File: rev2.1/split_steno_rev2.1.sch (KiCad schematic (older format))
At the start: 59 parts, among them J1 USB_OTG, J2 Audio-Jack-4, P1 TC2030-IDC, SW1 SW_Push, SW10 SW_Push, SW11 SW_Push, SW12 SW_Push, SW13 SW_Push, SW14 SW_Push, SW15 SW_Push, SW16 SW_Push, SW17 SW_Push, SW18 SW_Push, SW19 SW_Push, SW2 SW_Push, SW20 SW_Push, SW21 SW_Push, SW22 Switch-6P-2S2T, SW3 SW_Push, SW4 SW_Push, SW5 SW_Push, SW6 SW_Push, SW7 SW_Push, SW8 SW_Push, SW9 SW_Push, U1 74LVC1G34, U4 MCP1700, U5 ATXMEGA128A4U-AU, U6 nRF24L01_module

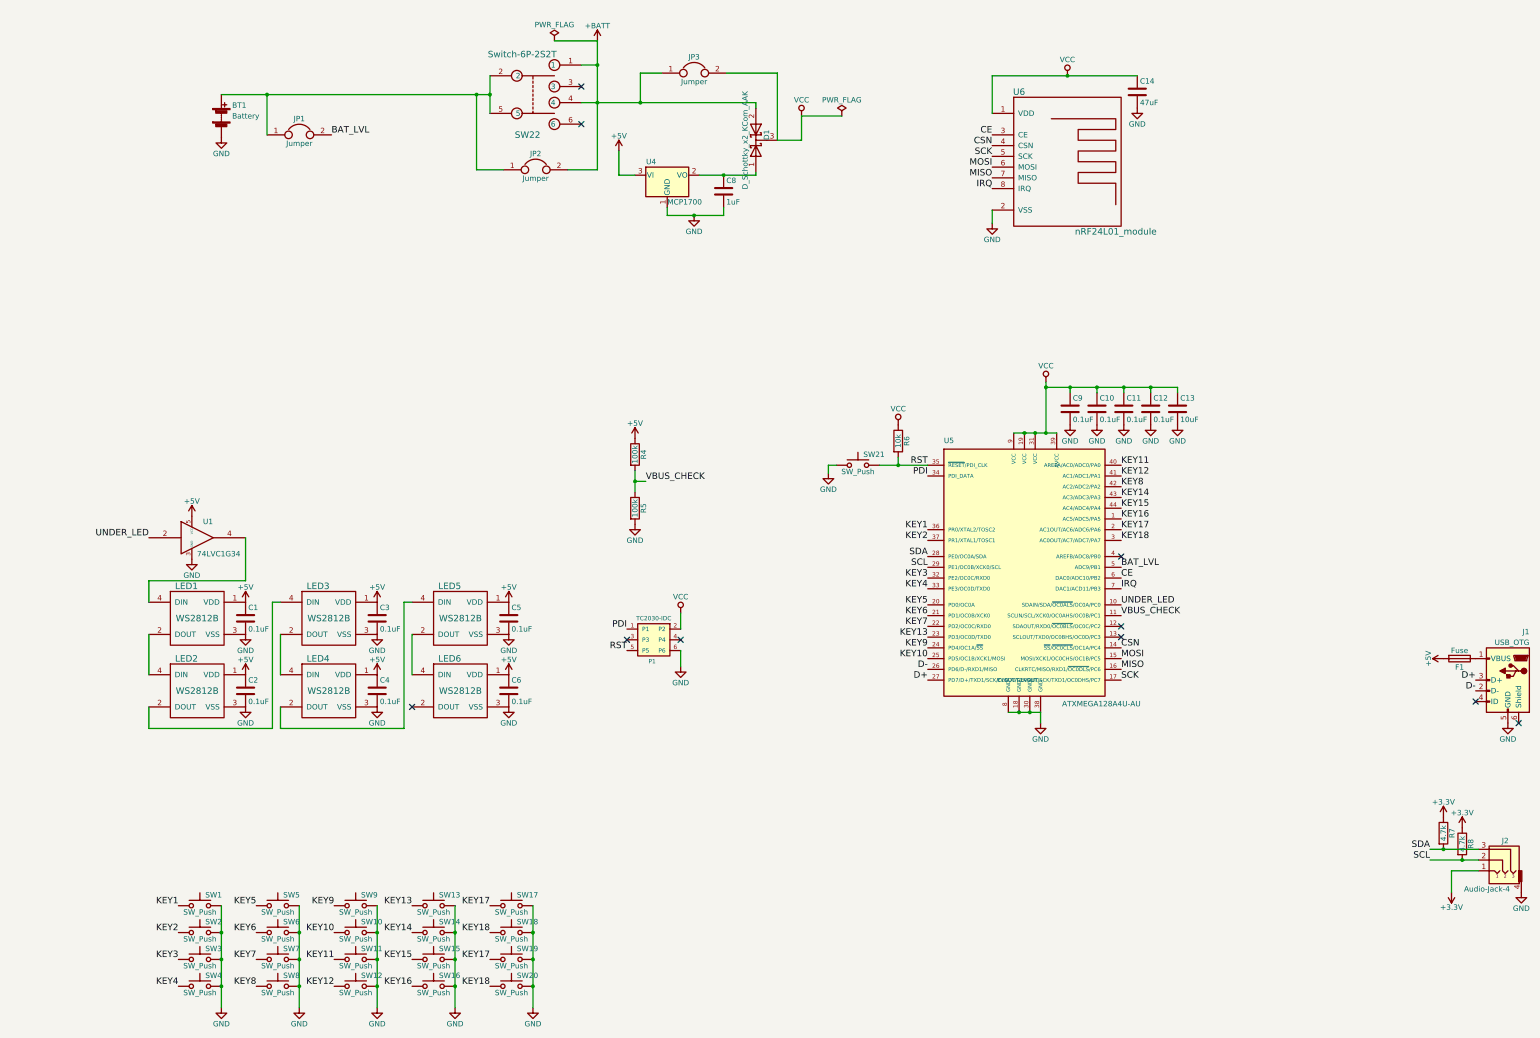
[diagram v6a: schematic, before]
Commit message: reorganized pins, removed NO USB jumper
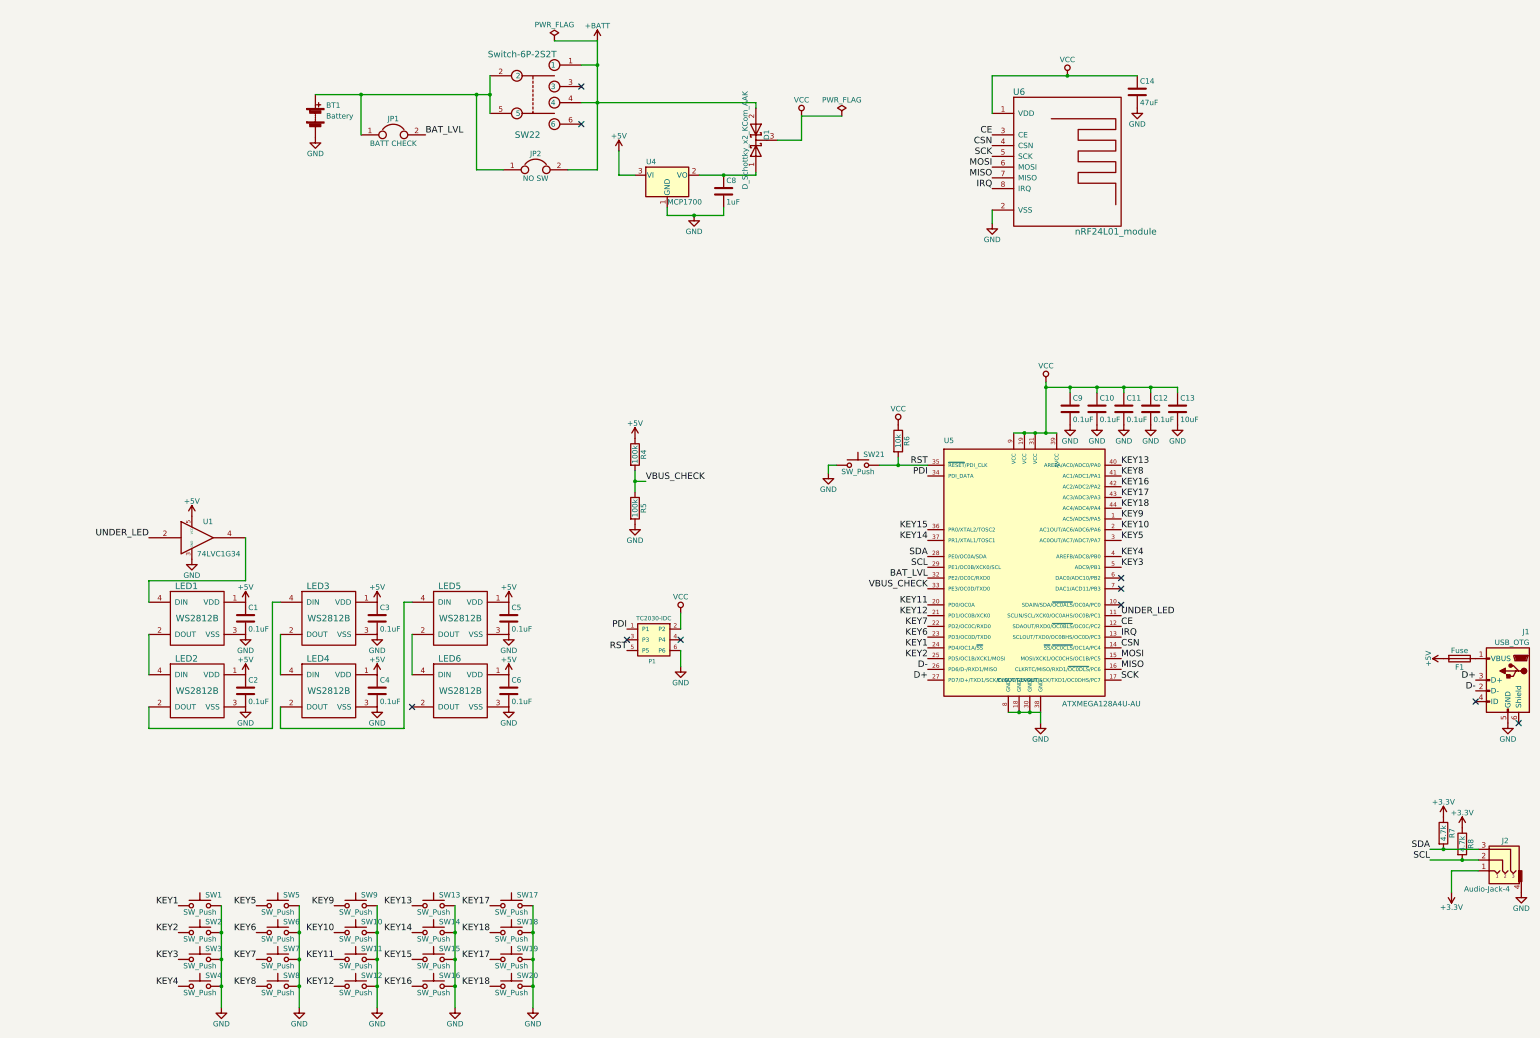
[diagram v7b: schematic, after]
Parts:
- removed JP3: Jumper, jumper:Jumper_1x02_P2.54mm_THT, symbol Jumper
- JP1: value Jumper -> BATT CHECK
- JP2: value Jumper -> NO SW
- P1: footprint Tag-Connect:TC2030-NL_SMALL_AND_IDC_PDI_Extra_Pads -> Tag-Connect:TC2030-NL_SMALL_AND_IDC_PDI
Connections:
- net BAT_LVL: now also U5.32 (PE2/OC0C/RXD0); no longer U5.5 (ADC9/PB1)
- net CE: now also U5.12 (SDAOUT/RXD0/~OC0BLS~/OC0C/PC2); no longer U5.6 (DAC0/ADC10/PB2)
- net IRQ: now also U5.13 (SCLOUT/TXD0/OC0BHS/OC0D/PC3); no longer U5.7 (DAC1/ACD11/PB3)
- net KEY1: now also U5.24 (PD4/OC1A/~SS~); no longer U5.36 (PR0/XTAL2/TOSC2)
- net KEY10: now also U5.2 (AC1OUT/AC6/ADC6/PA6); no longer U5.25 (PD5/OC1B/XCK1/MOSI)
- net KEY11: now also U5.20 (PD0/OC0A); no longer U5.40 (AREFA/AC0/ADC0/PA0)
- net KEY12: now also U5.21 (PD1/OC0B/XCK0); no longer U5.41 (AC1/ADC1/PA1)
- net KEY13: now also U5.40 (AREFA/AC0/ADC0/PA0); no longer U5.23 (PD3/OC0D/TXD0)
- net KEY14: now also U5.37 (PR1/XTAL1/TOSC1); no longer U5.43 (AC3/ADC3/PA3)
- net KEY15: now also U5.36 (PR0/XTAL2/TOSC2); no longer U5.44 (AC4/ADC4/PA4)
- net KEY16: now also U5.42 (AC2/ADC2/PA2); no longer U5.1 (AC5/ADC5/PA5)
- net KEY17: now also U5.43 (AC3/ADC3/PA3); no longer U5.2 (AC1OUT/AC6/ADC6/PA6)
- net KEY18: now also U5.44 (AC4/ADC4/PA4); no longer U5.3 (AC0OUT/AC7/ADC7/PA7)
- net KEY2: now also U5.25 (PD5/OC1B/XCK1/MOSI); no longer U5.37 (PR1/XTAL1/TOSC1)
- net KEY3: now also U5.5 (ADC9/PB1); no longer U5.32 (PE2/OC0C/RXD0)
- net KEY4: now also U5.4 (AREFB/ADC8/PB0); no longer U5.33 (PE3/OC0D/TXD0)
- net KEY5: now also U5.3 (AC0OUT/AC7/ADC7/PA7); no longer U5.20 (PD0/OC0A)
- net KEY6: now also U5.23 (PD3/OC0D/TXD0); no longer U5.21 (PD1/OC0B/XCK0)
- net KEY8: now also U5.41 (AC1/ADC1/PA1); no longer U5.42 (AC2/ADC2/PA2)
- net KEY9: now also U5.1 (AC5/ADC5/PA5); no longer U5.24 (PD4/OC1A/~SS~)
- net UNDER_LED: now also U5.11 (SCLIN/SCL/XCK0/OC0AHS/OC0B/PC1); no longer U5.10 (SDAIN/SDA/~OC0ALS~/OC0A/PC0)
- net VBUS_CHECK: now also U5.33 (PE3/OC0D/TXD0); no longer U5.11 (SCLIN/SCL/XCK0/OC0AHS/OC0B/PC1)
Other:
- moved on the sheet: BT1, JP1
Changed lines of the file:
@@
 	1    0    0    -1
 $EndComp
-Text Label 10875 6200 0    60   ~ 0
+Text Label 10875 6300 0    60   ~ 0
 UNDER_LED
 Text Label 10875 6600 0    60   ~ 0
@@
 Text Label 10875 6900 0    60   ~ 0
 SCK
-Text Label 10875 5950 0    60   ~ 0
+Text Label 10875 6400 0    60   ~ 0
 CE
-Text Label 10875 6050 0    60   ~ 0
+Text Label 10875 6500 0    60   ~ 0
 IRQ
 $Comp
 L Battery BT1
 U 1 1 5AB4F202
-P 2500 1650
-F 0 "BT1" H 2600 1750 50  0000 L CNN
-F 1 "Battery" H 2600 1650 50  0000 L CNN
-F 2 "battery:CR2032_BK-913" V 2500 1710 50  0001 C CNN
-F 3 "" V 2500 1710 50  0001 C CNN
-	1    2500 1650
+P 3375 1650
+F 0 "BT1" H 3475 1750 50  0000 L CNN
+F 1 "Battery" H 3475 1650 50  0000 L CNN
+F 2 "battery:CR2032_BK-913" V 3375 1710 50  0001 C CNN
+F 3 "" V 3375 1710 50  0001 C CNN
+	1    3375 1650
 	1    0    0    -1
 $EndComp
@@
 L GND #PWR023
 U 1 1 5AB4F4D8
-P 2500 1850
-F 0 "#PWR023" H 2500 1600 50  0001 C CNN
-F 1 "GND" H 2500 1700 50  0000 C CNN
-F 2 "" H 2500 1850 50  0001 C CNN
-F 3 "" H 2500 1850 50  0001 C CNN
-	1    2500 1850
+P 3375 1850
+F 0 "#PWR023" H 3375 1600 50  0001 C CNN
+F 1 "GND" H 3375 1700 50  0000 C CNN
+F 2 "" H 3375 1850 50  0001 C CNN
+F 3 "" H 3375 1850 50  0001 C CNN
+	1    3375 1850
 	1    0    0    -1
 $EndComp
@@
 L Jumper JP1
 U 1 1 5AB4F754
-P 3225 1825
-F 0 "JP1" H 3225 1975 50  0000 C CNN
-F 1 "Jumper" H 3225 1745 50  0000 C CNN
-F 2 "jumper:Jumper_1x02_P2.54mm_THT" H 3225 1825 50  0001 C CNN
-F 3 "" H 3225 1825 50  0001 C CNN
-	1    3225 1825
+P 4100 1825
+F 0 "JP1" H 4100 1975 50  0000 C CNN
+F 1 "BATT CHECK" H 4100 1745 50  0000 C CNN
+F 2 "jumper:Jumper_1x02_P2.54mm_THT" H 4100 1825 50  0001 C CNN
+F 3 "" H 4100 1825 50  0001 C CNN
+	1    4100 1825
 	1    0    0    -1
 $EndComp
@@
 P 5425 2150
 F 0 "JP2" H 5425 2300 50  0000 C CNN
-F 1 "Jumper" H 5425 2070 50  0000 C CNN
+F 1 "NO SW" H 5425 2070 50  0000 C CNN
 F 2 "jumper:Jumper_1x02_P2.54mm_THT" H 5425 2150 50  0001 C CNN
 F 3 "" H 5425 2150 50  0001 C CNN
@@
 	1    0    0    -1
 $EndComp
-$Comp
-L Jumper JP3
-U 1 1 5AB5FC00
-P 6900 1250
-F 0 "JP3" H 6900 1400 50  0000 C CNN
-F 1 "Jumper" H 6900 1170 50  0000 C CNN
-F 2 "jumper:Jumper_1x02_P2.54mm_THT" H 6900 1250 50  0001 C CNN
-F 3 "" H 6900 1250 50  0001 C CNN
-	1    6900 1250
-	1    0    0    -1
-$EndComp
 NoConn ~ 5850 1375
 NoConn ~ 5850 1725
-Text Label 3525 1825 0    60   ~ 0
+Text Label 4400 1825 0    60   ~ 0
 BAT_LVL
 $Comp
@@
 	1    0    0    -1
 $EndComp
-Text Label 10875 6300 0    60   ~ 0
+Text Label 9075 6050 2    60   ~ 0
 VBUS_CHECK
 $Comp
@@
 F 0 "P1" H 6475 6325 40  0000 L CNN
 F 1 "TC2030-IDC" H 6525 6725 40  0000 C CNN
-F 2 "Tag-Connect:TC2030-NL_SMALL_AND_IDC_PDI_Extra_Pads" H 6525 6525 60  0001 C CNN
+F 2 "Tag-Connect:TC2030-NL_SMALL_AND_IDC_PDI" H 6525 6525 60  0001 C CNN
 F 3 "" H 6525 6525 60  0001 C CNN
 	1    6525 6525
@@
 Connection ~ 10400 4175
 Wire Wire Line
-	2925 1825 2925 1450
-Wire Wire Line
-	2500 1450 5000 1450
-Connection ~ 2925 1450
+	3800 1825 3800 1450
+Connection ~ 3800 1450
 Wire Wire Line
 	5000 1275 5000 1625
@@
 Wire Wire Line
 	7900 1650 8275 1650
-Wire Wire Line
-	6600 1250 6400 1250
-Wire Wire Line
-	6400 1250 6400 1525
-Connection ~ 6400 1525
-Wire Wire Line
-	7200 1250 7675 1250
-Wire Wire Line
-	7675 1250 7675 1875
 Wire Wire Line
 	6775 6425 6775 6275
@@
 Text Label 9075 6900 2    60   ~ 0
 D+
-Text Label 9075 5500 2    60   ~ 0
+Text Label 9075 6600 2    60   ~ 0
 KEY1
-Text Label 9075 5600 2    60   ~ 0
+Text Label 9075 6700 2    60   ~ 0
 KEY2
-Text Label 9075 5950 2    60   ~ 0
+Text Label 10875 5850 0    60   ~ 0
 KEY3
-Text Label 9075 6050 2    60   ~ 0
+Text Label 10875 5750 0    60   ~ 0
 KEY4
-Text Label 9075 6200 2    60   ~ 0
+Text Label 10875 5600 0    60   ~ 0
 KEY5
-Text Label 9075 6300 2    60   ~ 0
+Text Label 9075 6500 2    60   ~ 0
 KEY6
 Text Label 9075 6400 2    60   ~ 0
 KEY7
+Text Label 10875 5000 0    60   ~ 0
+KEY8
+Text Label 10875 5400 0    60   ~ 0
+KEY9
+Text Label 10875 5500 0    60   ~ 0
+KEY10
+Text Label 9075 6200 2    60   ~ 0
+KEY11
+Text Label 9075 6300 2    60   ~ 0
+KEY12
+Text Label 10875 4900 0    60   ~ 0
+KEY13
+Text Label 9075 5600 2    60   ~ 0
+KEY14
+Text Label 9075 5500 2    60   ~ 0
+KEY15
 Text Label 10875 5100 0    60   ~ 0
-KEY8
-Text Label 9075 6600 2    60   ~ 0
-KEY9
-Text Label 9075 6700 2    60   ~ 0
-KEY10
-Text Label 10875 4900 0    60   ~ 0
-KEY11
-Text Label 10875 5000 0    60   ~ 0
-KEY12
-Text Label 9075 6500 2    60   ~ 0
-KEY13
+KEY16
 Text Label 10875 5200 0    60   ~ 0
-KEY14
+KEY17
 Text Label 10875 5300 0    60   ~ 0
-KEY15
-Text Label 10875 5400 0    60   ~ 0
-KEY16
-Text Label 10875 5500 0    60   ~ 0
-KEY17
-Text Label 10875 5600 0    60   ~ 0
 KEY18
-NoConn ~ 10875 5750
+NoConn ~ 10875 6200
 $Comp
 L Fuse F1
@@
 Wire Wire Line
 	3050 7350 3050 7150
-Text Label 10875 5850 0    60   ~ 0
+Text Label 9075 5950 2    60   ~ 0
 BAT_LVL
-NoConn ~ 10875 6400
-NoConn ~ 10875 6500
+NoConn ~ 10875 5950
+NoConn ~ 10875 6050
+Wire Wire Line
+	3375 1450 5000 1450
 $EndSCHEMATC

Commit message: laid out components
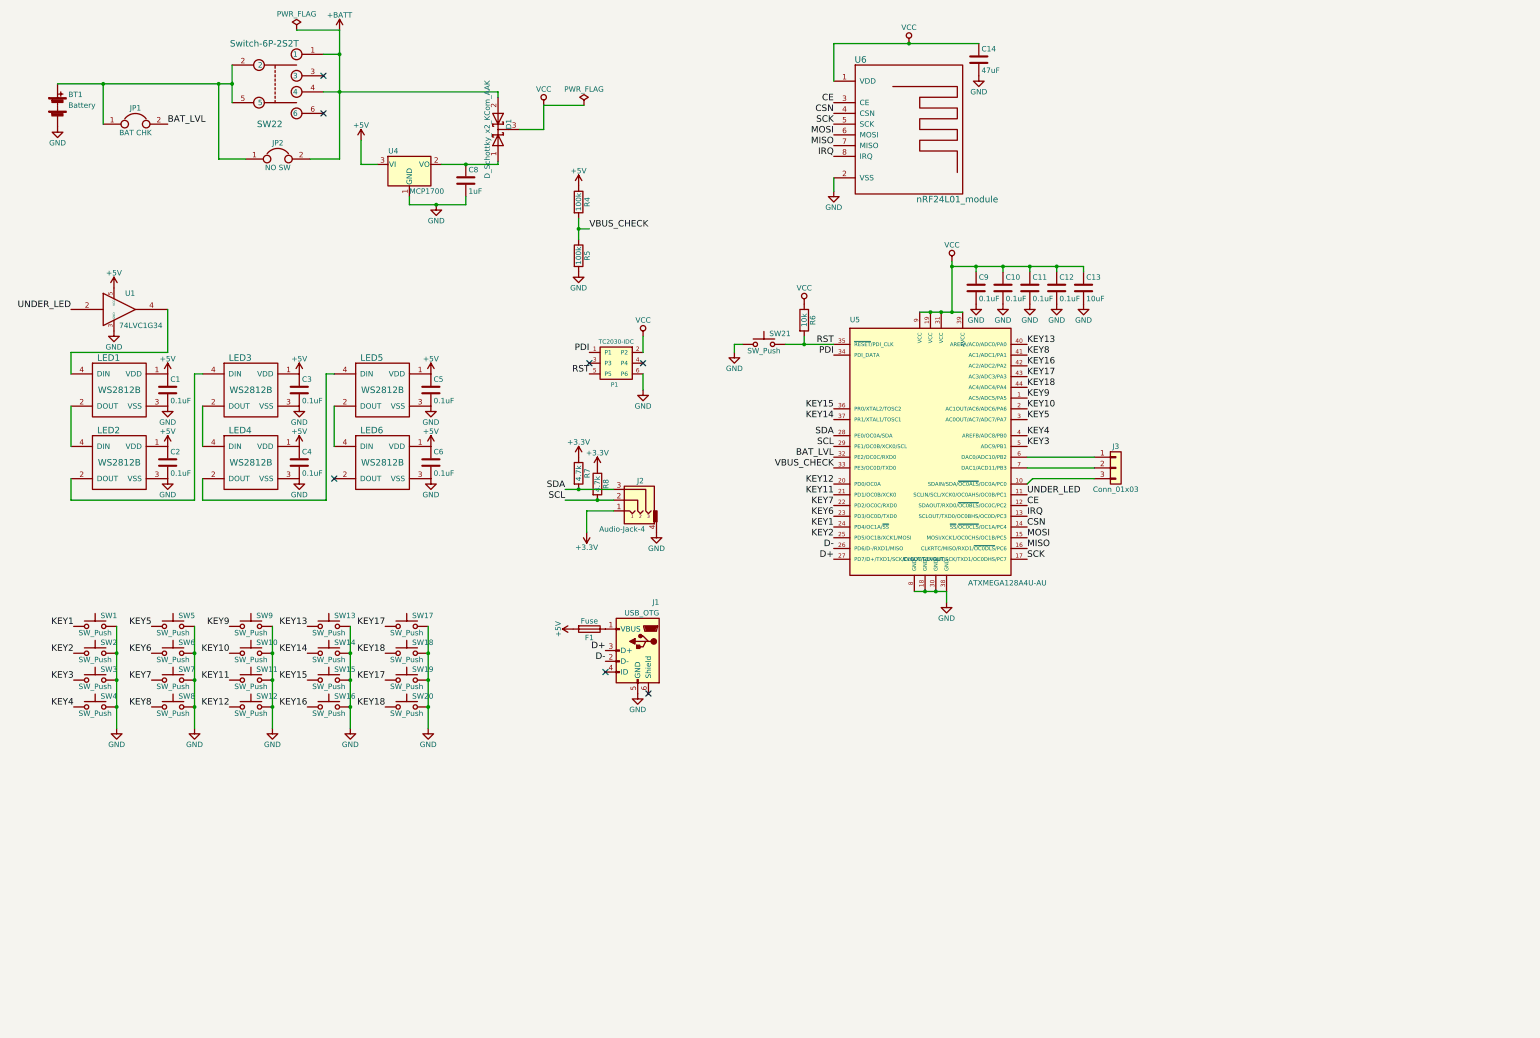
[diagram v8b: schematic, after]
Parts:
- added J3: Conn_01x03, Pin_Headers:Pin_Header_Straight_1x03_Pitch2.54mm, symbol Conn_01x03
- JP1: value BATT CHECK -> BAT CHK
- SW14, SW3, SW4, SW7: footprint Keebio-Parts:Hybrid_PCB_100H_Dual_hole -> Keebio-Parts:Hybrid_PCB_100H_Dual_hole-flip
- U4: footprint TO_SOT_Packages_SMD:SOT-23 -> TO_SOT_Packages_SMD:SOT-23_Handsoldering
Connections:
- net KEY11: now also U5.21 (PD1/OC0B/XCK0); no longer U5.20 (PD0/OC0A)
- net KEY12: now also U5.20 (PD0/OC0A); no longer U5.21 (PD1/OC0B/XCK0)
- net at U5.10 (SDAIN/SDA/~OC0ALS~/OC0A/PC0): now also J3.3 (Pin_3)
- net at U5.6 (DAC0/ADC10/PB2): now also J3.1 (Pin_1)
- net at U5.7 (DAC1/ACD11/PB3): now also J3.2 (Pin_2)
- no-connect marks 10 -> 7
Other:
- moved on the sheet: BT1, C1, C10, C11, C12, C13, C14, C2, C3, C4, C5, C6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
